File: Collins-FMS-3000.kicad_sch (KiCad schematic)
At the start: 35 parts, among them U2 MCP23017_SO, U3 MCP23017_SO, U4 IS31FL3733B

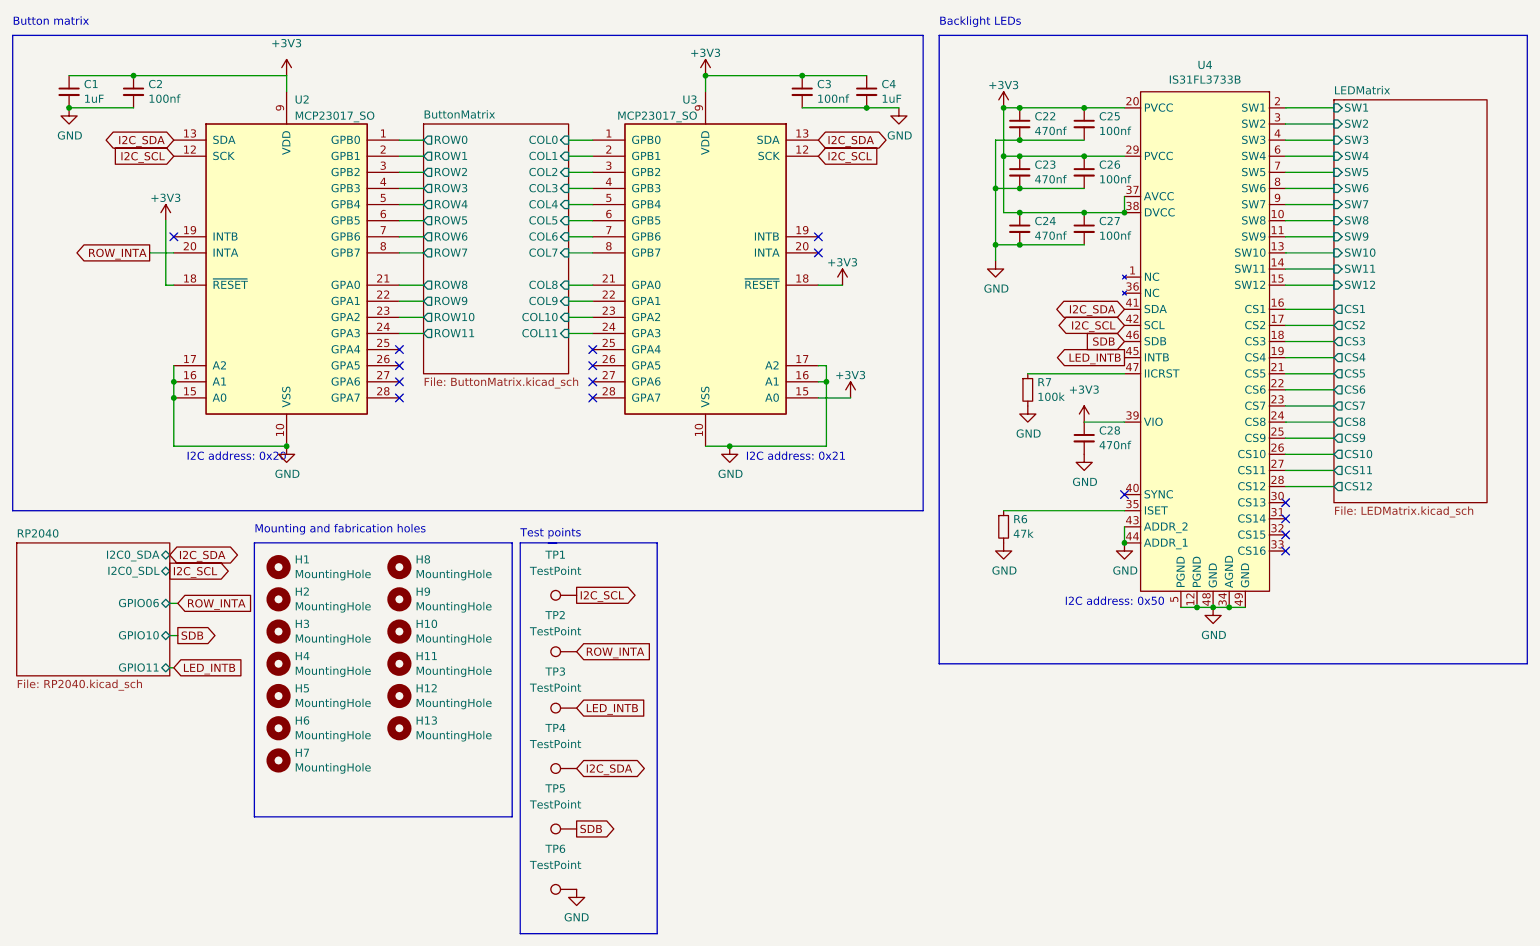
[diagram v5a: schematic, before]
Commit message: Keyboard driver (#25)
* Lots of pre-work before replacing RP2040 layout

* New RP2040 layout added

* FULLY ROUTED

* Clean up schematic

* More trace cleanup

* Final trace cleanup

Co-authored-by: Neil Enns <{ID}+{username}@users.noreply.github.com>
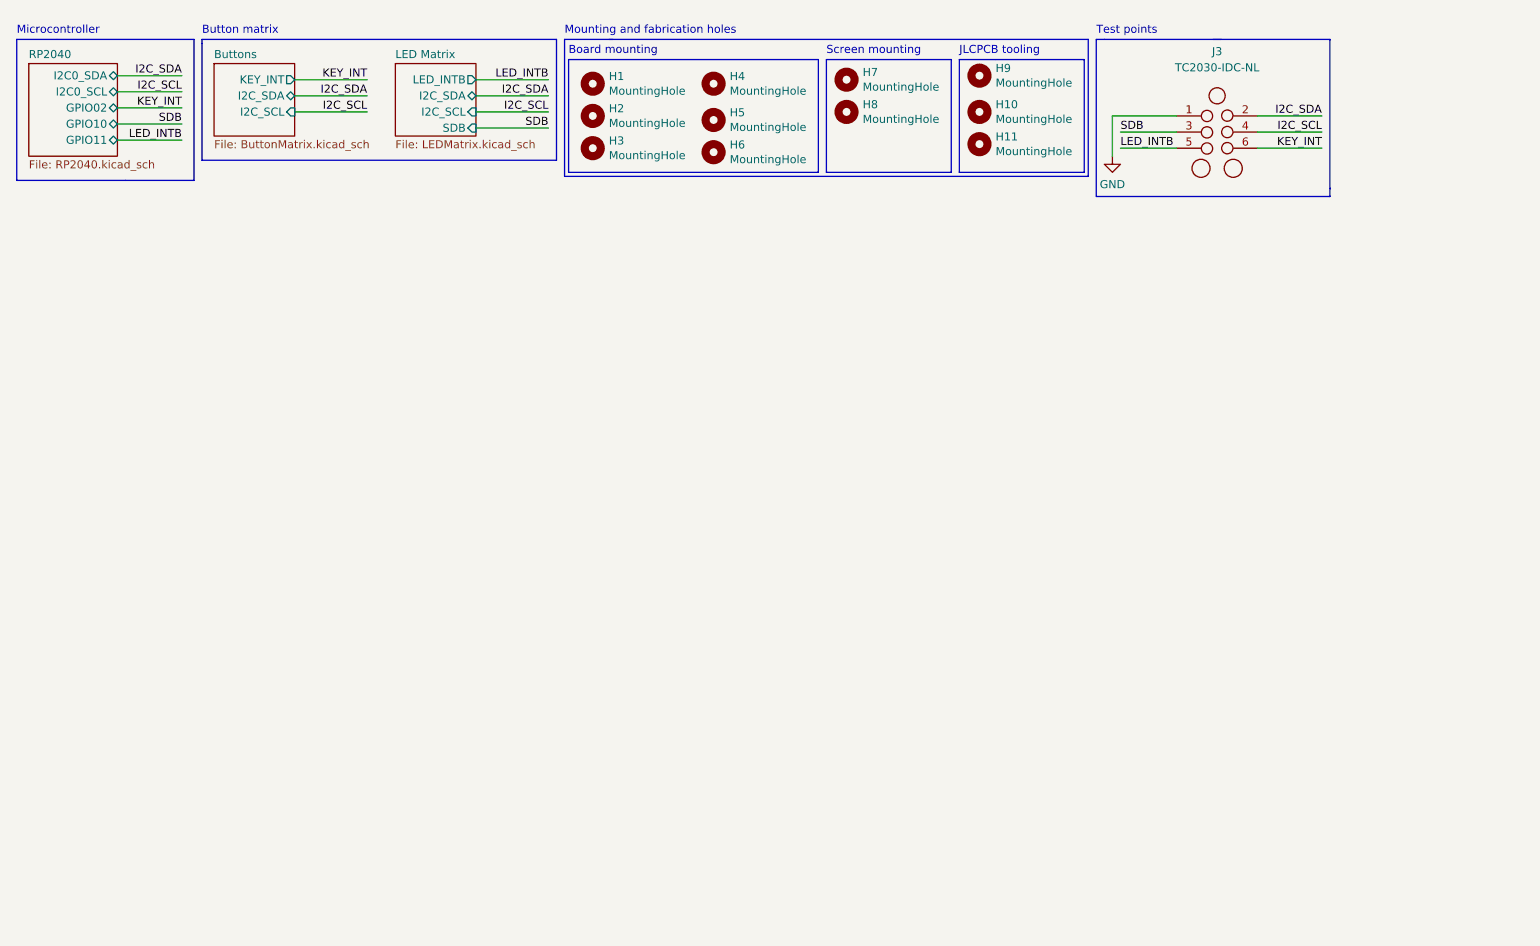
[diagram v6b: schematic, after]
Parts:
- removed C1, C4: 1uF, Collins-FMS-3000:Perfect_0402, symbol Device:C_Small
- removed C2, C25, C26, C27, C3: 100nf, Collins-FMS-3000:Perfect_0402, symbol Device:C_Small
- removed C22, C23, C24, C28: 470nf, Collins-FMS-3000:Perfect_0402, symbol Device:C_Small
- removed H4: MountingHole, MountingHole:MountingHole_3.2mm_M3, symbol Mechanical:MountingHole
- removed H5, H6: MountingHole, Collins-FMS-3000:JLCPCB_Tooling_Hole, symbol Mechanical:MountingHole
- removed R6: 47k, Collins-FMS-3000:Perfect_0402, symbol Device:R_Small
- removed R7: 100k, Resistor_SMD:R_0603_1608Metric, symbol Device:R_Small
- removed TP1, TP2, TP3, TP4, TP5, TP6: TestPoint, TestPoint:TestPoint_Keystone_5005-5009_Compact, symbol Connector:TestPoint
- removed U2, U3: MCP23017_SO, Package_SO:SOIC-28W_7.5x17.9mm_P1.27mm, symbol Interface_Expansion:MCP23017_SO
- removed U4: IS31FL3733B, Package_QFP:TQFP-48-1EP_7x7mm_P0.5mm_EP5x5mm_ThermalVias, symbol Collins-FMS-3000:IS31FL3733B
- added H7: MountingHole, MountingHole:MountingHole_3.2mm_M3, symbol Mechanical:MountingHole
- added J3: TC2030-IDC-NL, Connector:Tag-Connect_TC2030-IDC-NL_2x03_P1.27mm_Vertical, symbol Custom_Symbols:TC2030-IDC-NL
- H11: renamed from H13; footprint MountingHole:MountingHole_3.2mm_M3 -> Collins-FMS-3000:JLCPCB_Tooling_Hole
- H9: footprint MountingHole:MountingHole_3.2mm_M3 -> Collins-FMS-3000:JLCPCB_Tooling_Hole
- renumbered H7 to H10, H10 to H4, H11 to H5, H12 to H6
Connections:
- net GND: now also J3.1 (Pin_1)
- net I2C_SCL: now also J3.4 (Pin_4)
- net I2C_SDA: now also J3.2 (Pin_2)
- net LED_INTB: now also J3.5 (Pin_5)
- net SDB: now also J3.3 (Pin_3)
- new net KEY_INT: J3.6 (Pin_6)
- no-connect marks 16 -> 0
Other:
- sheet ButtonMatrix renamed Buttons
- sheet LEDMatrix renamed LED Matrix
- sheet Buttons ports: added I2C_SCL, I2C_SDA, KEY_INT; removed COL0, COL1, COL10, COL11, COL2, COL3, COL4, COL5, COL6, COL7, COL8, COL9, ROW0, ROW1, ROW10, ROW11, ROW2, ROW3, ROW4, ROW5, ROW6, ROW7, ROW8, ROW9
- sheet LED Matrix ports: added I2C_SCL, I2C_SDA, LED_INTB, SDB; removed CS1, CS10, CS11, CS12, CS2, CS3, CS4, CS5, CS6, CS7, CS8, CS9, SW1, SW10, SW11, SW12, SW2, SW3, SW4, SW5, SW6, SW7, SW8, SW9
- sheet RP2040 ports: added GPIO02, I2C0_SCL; removed GPIO06, I2C0_SDL
- note added: "Board mounting"
- note added: "JLCPCB tooling"
- note added: "Microcontroller"
- note added: "Screen mounting"
- note removed: "Backlight LEDs"
- note removed: "I2C address: 0x20"
- note removed: "I2C address: 0x21"
- note removed: "I2C address: 0x50"
- moved on the sheet: H1, H10, H11, H2, H3, H4, H5, H6
